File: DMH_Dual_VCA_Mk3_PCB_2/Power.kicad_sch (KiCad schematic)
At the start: 14 parts, among them J100 IDC_02x05, U1 TL074, U2 TL074, U3 TL072

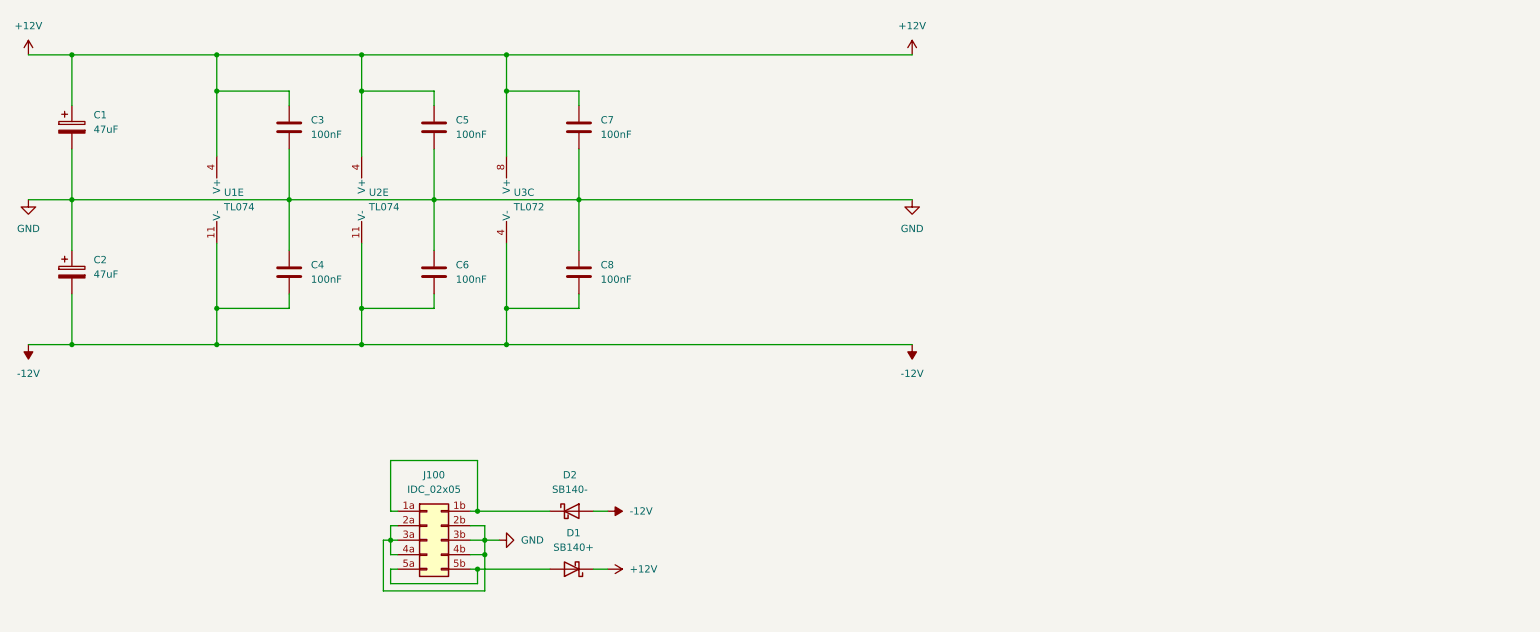
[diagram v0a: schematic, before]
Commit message: Synced PCB 1 and 2 schematics
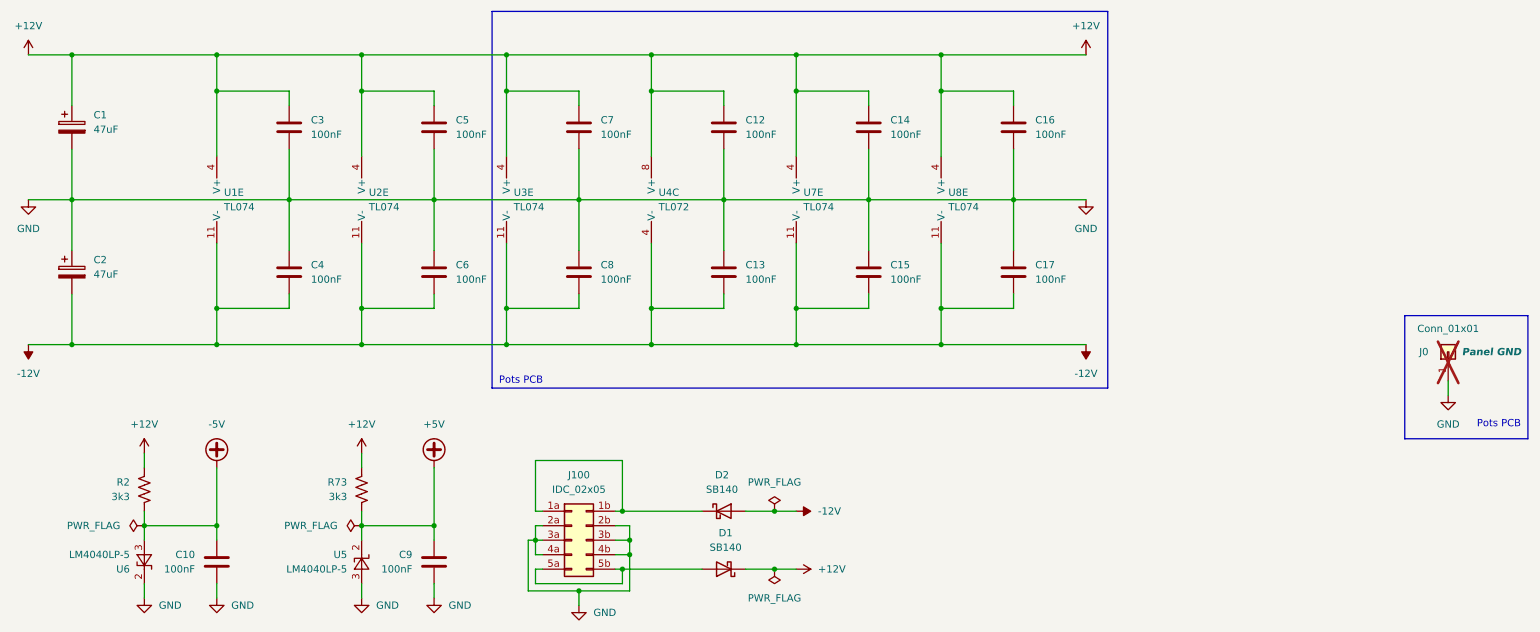
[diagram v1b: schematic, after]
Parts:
- removed U3: TL072, Package_DIP:DIP-8_W7.62mm_Socket, symbol Amplifier_Operational:TL072
- added C10, C12, C13, C14, C15, C16, C17, C9: 100nF, Capacitor_THT:C_Disc_D4.3mm_W1.9mm_P5.00mm, symbol Device:C
- added J0: Conn_01x01, Connector_PinHeader_2.54mm:PinHeader_1x01_P2.54mm_Vertical, symbol Connector_Generic:Conn_01x01
- added R2, R73: 3k3, Resistor_THT:R_Axial_DIN0207_L6.3mm_D2.5mm_P7.62mm_Horizontal, symbol Device:R_US
- added U3, U7, U8: TL074, Package_DIP:DIP-14_W7.62mm_Socket, symbol Amplifier_Operational:TL074
- added U4: TL072, Package_DIP:DIP-8_W7.62mm_Socket, symbol Amplifier_Operational:TL072
- added U5, U6: LM4040LP-5, Package_TO_SOT_THT:TO-92_Inline, symbol Reference_Voltage:LM4040LP-5
- D1: value SB140+ -> SB140; symbol SynthStuff:Power_Bus_Schotty_+ -> Diode:SB140
- D2: value SB140- -> SB140; symbol SynthStuff:Power_Bus_Schotty_- -> Diode:SB140
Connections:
- net +12V: now also C12.1, C14.1, C16.1, R2.2, R73.2, U3.4 (V+), U4.8 (V+), U7.4 (V+), U8.4 (V+)
- net -12V: now also C13.2, C15.2, C17.2, U3.11 (V-), U4.4 (V-), U7.11 (V-), U8.11 (V-)
- net GND: now also C10.2, C12.2, C13.1, C14.2, C15.1, C16.2, C17.1, C9.2, J0.1 (Pin_1), U5.3 (A), U6.2 (K)
- new net +5V: C9.1, R73.1, U5.2 (K)
- new net -5V: C10.1, R2.1, U6.3 (A)
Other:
- note added: "Pots PCB"
- moved on the sheet: D1, D2, J100

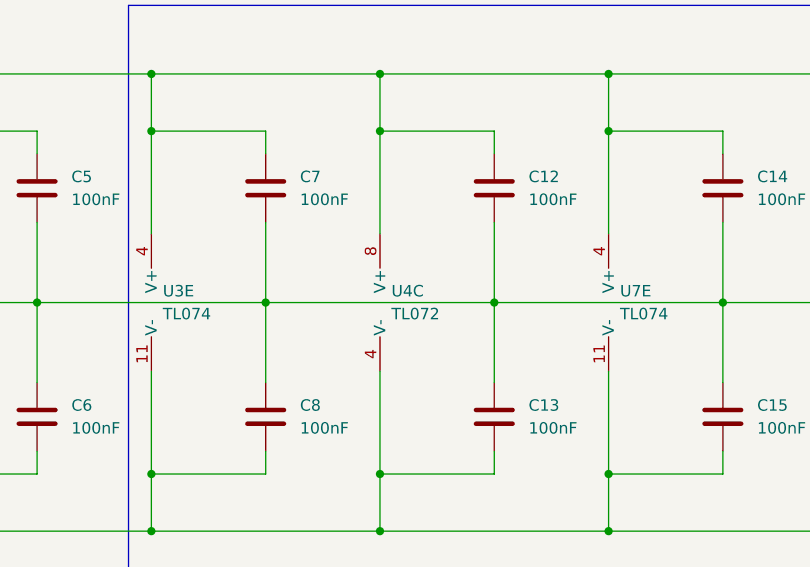
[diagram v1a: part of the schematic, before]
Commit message: Added clipping LED to schematic
Still need to add to Panel
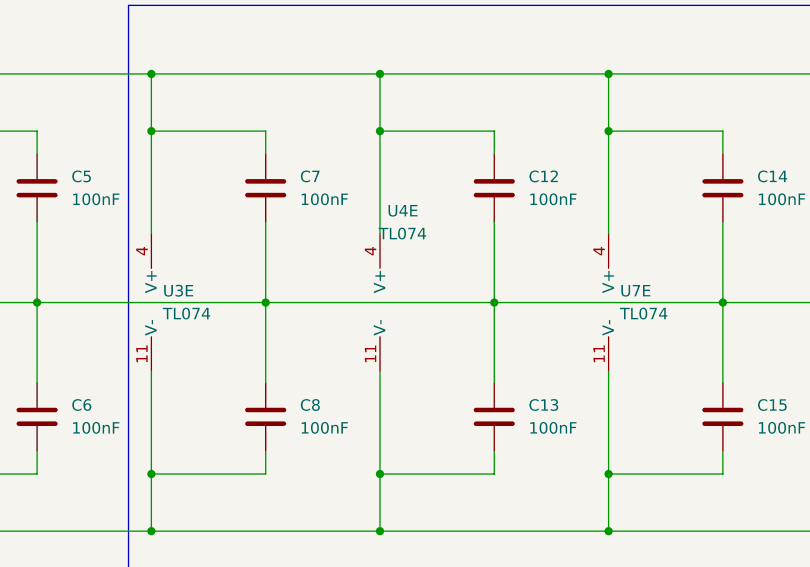
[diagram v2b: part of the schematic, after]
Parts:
- U4: value TL072 -> TL074; footprint Package_DIP:DIP-8_W7.62mm_Socket -> Package_DIP:DIP-14_W7.62mm_Socket; symbol Amplifier_Operational:TL072 -> Amplifier_Operational:TL074
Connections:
- net +12V: now also U4.4 (V+); no longer U4.8 (V+)
- net -12V: now also U4.11 (V-); no longer U4.4 (V-)
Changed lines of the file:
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@@
 	)
 	(symbol
-		(lib_id "Amplifier_Operational:TL072")
+		(lib_id "Amplifier_Operational:TL074")
 		(at 129.54 120.65 0)
-		(unit 3)
+		(unit 5)
 		(exclude_from_sim no)
 		(in_bom yes)
@@
 		(fields_autoplaced yes)
 		(property "Reference" "U4"
-			(at 128.27 119.3799 0)
+			(at 129.54 110.49 0)
 			(effects
 				(font
 					(size 1.27 1.27)
 				)
-				(justify left)
 			)
 		)
-		(property "Value" "TL072"
-			(at 128.27 121.9199 0)
+		(property "Value" "TL074"
+			(at 129.54 113.03 0)
 			(effects
 				(font
 					(size 1.27 1.27)
 				)
-				(justify left)
 			)
 		)
-		(property "Footprint" "Package_DIP:DIP-8_W7.62mm_Socket"
+		(property "Footprint" "Package_DIP:DIP-14_W7.62mm_Socket"
+			(at 128.27 118.11 0)
+			(effects
+				(font
+					(size 1.27 1.27)
+				)
+				(hide yes)
+			)
+		)
+		(property "Datasheet" "http://www.ti.com/lit/ds/symlink/tl071.pdf"
+			(at 130.81 115.57 0)
+			(effects
+				(font
+					(size 1.27 1.27)
+				)
+				(hide yes)
+			)
+		)
+		(property "Description" "Quad Low-Noise JFET-Input Operational Amplifiers, DIP-14/SOIC-14"
 			(at 129.54 120.65 0)
 			(effects
@@
 			)
 		)
-		(property "Datasheet" "http://www.ti.com/lit/ds/symlink/tl071.pdf"
+		(property "Function" ""
 			(at 129.54 120.65 0)
 			(effects
@@
 					(size 1.27 1.27)
 				)
-				(hide yes)
-			)
-		)
-		(property "Description" "Dual Low-Noise JFET-Input Operational Amplifiers, DIP-8/SOIC-8"
-			(at 129.54 120.65 0)
-			(effects
-				(font
-					(size 1.27 1.27)
-				)
-				(hide yes)
 			)
 		)
@@
 		(pin "4"
 		)
+		(pin "10"
+		)
+		(pin "9"
+		)
+		(pin "13"
+		)
+		(pin "12"
+		)
+		(pin "14"
+		)
+		(pin "11"
+		)
 		(instances
 			(project ""
 				(path "/58f4306d-5387-4983-bb08-41a2313fd315/0cdf34b2-39cd-4d9e-981a-97cd34791509"
 					(reference "U4")
-					(unit 3)
+					(unit 5)
 				)
 			)

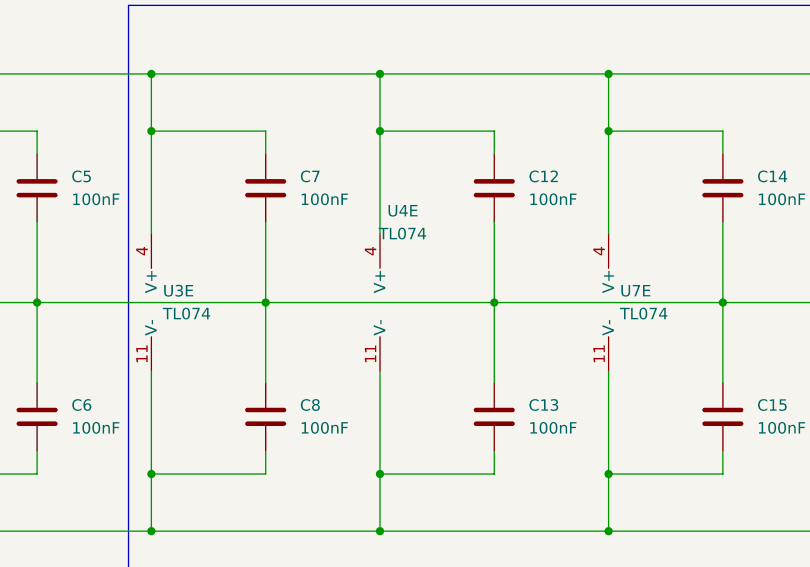
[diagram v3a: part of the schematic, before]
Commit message: Improved clipping indicator
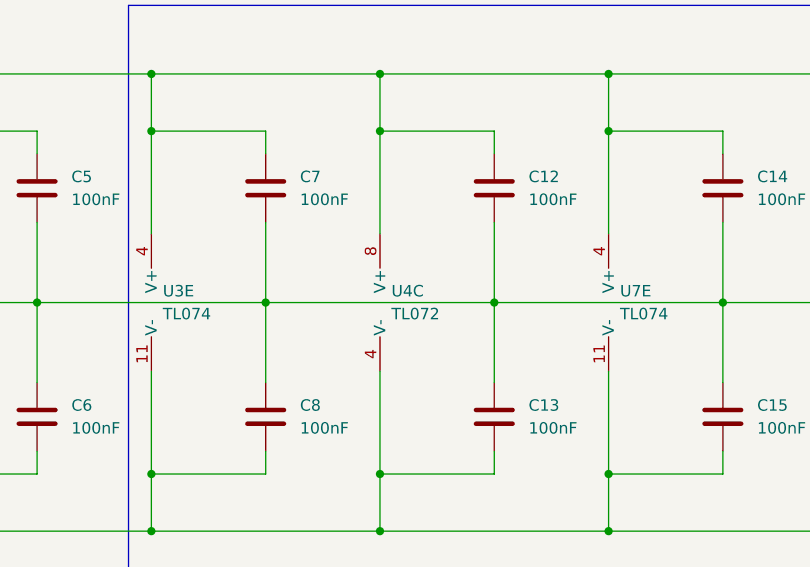
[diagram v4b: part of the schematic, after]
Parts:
- removed U4: TL074, Package_DIP:DIP-14_W7.62mm_Socket, symbol Amplifier_Operational:TL074
- added U4: TL072, Package_DIP:DIP-8_W7.62mm_Socket, symbol Amplifier_Operational:TL072
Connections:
- net +12V: now also U4.8 (V+)
- net -12V: now also U4.4 (V-)
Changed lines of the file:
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@@
-	)
-	(symbol
-		(lib_id "Amplifier_Operational:TL074")
-		(at 129.54 120.65 0)
-		(unit 5)
-		(exclude_from_sim no)
-		(in_bom yes)
-		(on_board yes)
-		(dnp no)
-		(fields_autoplaced yes)
-		(property "Reference" "U4"
-			(at 129.54 110.49 0)
-			(effects
-				(font
-					(size 1.27 1.27)
-				)
-			)
-		)
-		(property "Value" "TL074"
-			(at 129.54 113.03 0)
-			(effects
-				(font
-					(size 1.27 1.27)
-				)
-			)
-		)
-		(property "Footprint" "Package_DIP:DIP-14_W7.62mm_Socket"
-			(at 128.27 118.11 0)
-			(effects
-				(font
-					(size 1.27 1.27)
-				)
-				(hide yes)
-			)
-		)
-		(property "Datasheet" "http://www.ti.com/lit/ds/symlink/tl071.pdf"
-			(at 130.81 115.57 0)
-			(effects
-				(font
-					(size 1.27 1.27)
-				)
-				(hide yes)
-			)
-		)
-		(property "Description" "Quad Low-Noise JFET-Input Operational Amplifiers, DIP-14/SOIC-14"
-			(at 129.54 120.65 0)
-			(effects
-				(font
-					(size 1.27 1.27)
-				)
-				(hide yes)
-			)
-		)
-		(property "Function" ""
-			(at 129.54 120.65 0)
-			(effects
-				(font
-					(size 1.27 1.27)
-				)
-			)
-		)
-		(pin "1"
-		)
-		(pin "7"
-		)
-		(pin "2"
-		)
-		(pin "3"
-		)
-		(pin "5"
-		)
-		(pin "6"
-		)
-		(pin "8"
-		)
-		(pin "4"
-		)
-		(pin "10"
-		)
-		(pin "9"
-		)
-		(pin "13"
-		)
-		(pin "12"
-		)
-		(pin "14"
-		)
-		(pin "11"
-		)
-		(instances
-			(project ""
-				(path "/58f4306d-5387-4983-bb08-41a2313fd315/0cdf34b2-39cd-4d9e-981a-97cd34791509"
-					(reference "U4")
-					(unit 5)
-				)
-			)
-		)
 	)
 	(symbol
@@
 				)
 			)
+		)
+	)
+	(symbol
+		(lib_id "Amplifier_Operational:TL072")
+		(at 129.54 120.65 0)
+		(unit 3)
+		(exclude_from_sim no)
+		(in_bom yes)
+		(on_board yes)
+		(dnp no)
+		(fields_autoplaced yes)
+		(property "Reference" "U4"
+			(at 128.27 119.3799 0)
+			(effects
+				(font
+					(size 1.27 1.27)
+				)
+				(justify left)
+			)
+		)
+		(property "Value" "TL072"
+			(at 128.27 121.9199 0)
+			(effects
+				(font
+					(size 1.27 1.27)
+				)
+				(justify left)
+			)
+		)
+		(property "Footprint" "Package_DIP:DIP-8_W7.62mm_Socket"
+			(at 129.54 120.65 0)
+			(effects
+				(font
+					(size 1.27 1.27)
+				)
+				(hide yes)
+			)
+		)
+		(property "Datasheet" "http://www.ti.com/lit/ds/symlink/tl071.pdf"
+			(at 129.54 120.65 0)
+			(effects
+				(font
+					(size 1.27 1.27)
+				)
+				(hide yes)
+			)
+		)
+		(property "Description" "Dual Low-Noise JFET-Input Operational Amplifiers, DIP-8/SOIC-8"
+			(at 129.54 120.65 0)
+			(effects
+				(font
+					(size 1.27 1.27)
+				)
+				(hide yes)
+			)
+		)
+		(pin "6"
+		)
+		(pin "7"
+		)
+		(pin "8"
+		)
+		(pin "4"
+		)
+		(pin "3"
+		)
+		(pin "2"
+		)
+		(pin "1"
+		)
+		(pin "5"
+		)
+		(instances
+			(project "DMH_Dual_VCA_Mk3_PCB_2"
+				(path "/58f4306d-5387-4983-bb08-41a2313fd315/0cdf34b2-39cd-4d9e-981a-97cd34791509"
+					(reference "U4")
+					(unit 3)
+				)
+			)
